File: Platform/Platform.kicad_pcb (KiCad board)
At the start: 2 copper layers, 70 x 107 mm, 0 parts

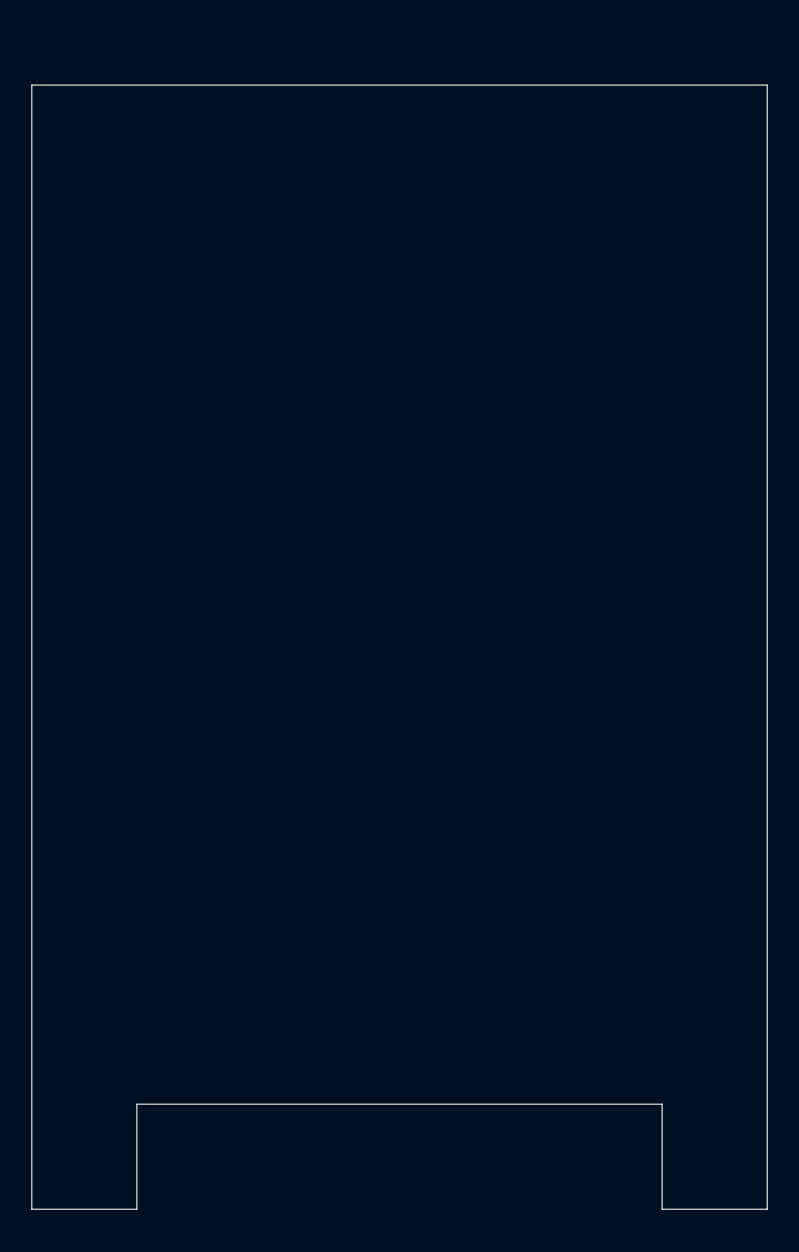
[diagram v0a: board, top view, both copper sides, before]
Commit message: Updated the PCB with component foot prints.
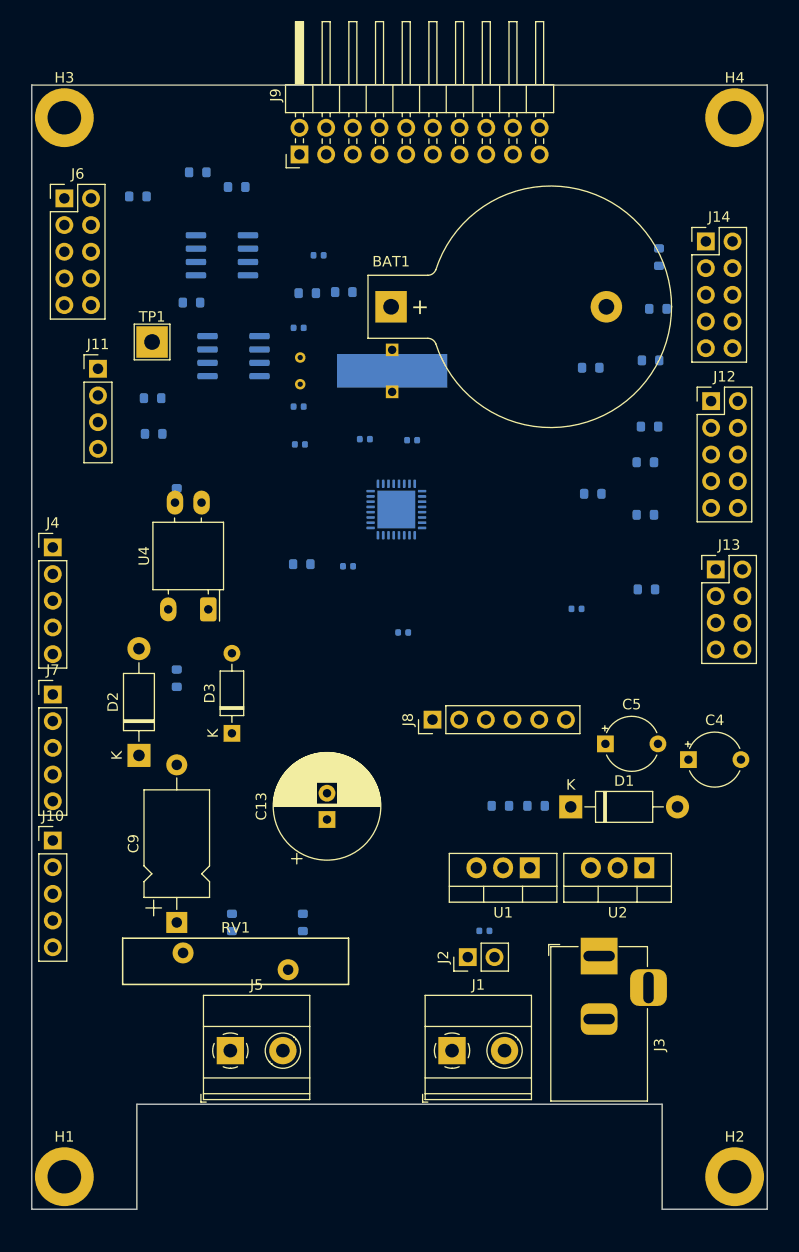
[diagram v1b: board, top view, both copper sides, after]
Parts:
- added BAT1: BS-7 3.3V, Battery:BatteryHolder_Keystone_103_1x20mm, F.Cu at (144.2, 71.2)
- added C1: 0.33uF 330NF-0402, Capacitor_SMD:C_0402_1005Metric, B.Cu at (145.3, 102.2)
- added C10: 0.1U to 1UF, Capacitor_SMD:C_0402_1005Metric, B.Cu at (137.3, 66.3)
- added C11: C_Small, Capacitor_SMD:C_0402_1005Metric, B.Cu at (135.4, 73.2)
- added C12: C_Small, Capacitor_SMD:C_0402_1005Metric, B.Cu at (135.4, 80.7)
- added C13: 2000uF, Capacitor_THT:CP_Radial_D10.0mm_P2.50mm, F.Cu at (138.1, 120.0)
- added C14: C_Small, Capacitor_SMD:C_0402_1005Metric, B.Cu at (140.1, 95.9)
- added C2: 0.1uF, Capacitor_SMD:C_0402_1005Metric, B.Cu at (161.8, 100.0)
- added C3: 0.1uF, Capacitor_SMD:C_0402_1005Metric, B.Cu at (153.1, 130.6)
- added C4: 10uF, Capacitor_THT:CP_Radial_Tantal_D5.0mm_P5.00mm, F.Cu at (172.5, 114.3)
- added C5: 1uF, Capacitor_THT:CP_Radial_Tantal_D5.0mm_P5.00mm, F.Cu at (164.6, 112.8)
- added C6: 100nF DNP, Capacitor_SMD:C_0402_1005Metric, B.Cu at (141.7, 83.8)
- added C7: 1uF, Capacitor_SMD:C_0402_1005Metric, B.Cu at (146.2, 83.9)
- added C8: 100nF DNP, Capacitor_SMD:C_0402_1005Metric, B.Cu at (135.5, 84.3)
- added C9: 0.47uF 450V AC 15mm Pitch, Capacitor_THT:CP_Axial_L10.0mm_D6.0mm_P15.00mm_Horizontal, F.Cu at (123.8, 129.8)
- added D1: 1N4001, Diode_THT:D_DO-41_SOD81_P10.16mm_Horizontal, F.Cu at (161.3, 118.8)
- added D2: DIODE IN4007, Diode_THT:D_DO-41_SOD81_P10.16mm_Horizontal, F.Cu at (120.2, 113.9)
- added D3: 5V_Zener, Diode_THT:D_DO-35_SOD27_P7.62mm_Horizontal, F.Cu at (129.1, 111.8)
- added H1: MountingHole, MountingHole:MountingHole_3.2mm_M3_DIN965_Pad, F.Cu at (113.1, 154.0)
- added H2: MountingHole, MountingHole:MountingHole_3.2mm_M3_DIN965_Pad, F.Cu at (176.9, 154.0)
- added H3: MountingHole, MountingHole:MountingHole_3.2mm_M3_DIN965_Pad, F.Cu at (113.1, 53.2)
- added H4: MountingHole, MountingHole:MountingHole_3.2mm_M3_DIN965_Pad, F.Cu at (176.9, 53.2)
- added J1: 12V INPUT, TerminalBlock_Phoenix:TerminalBlock_Phoenix_MKDS-1,5-2_1x02_P5.00mm_Horizontal, F.Cu at (150.0, 142.0)
- added J10: Conn_01x05, Connector_PinHeader_2.54mm:PinHeader_1x05_P2.54mm_Vertical, F.Cu at (112.0, 122.0)
- added J11: Relay_conn, Connector_PinHeader_2.54mm:PinHeader_1x04_P2.54mm_Vertical, F.Cu at (116.3, 77.1)
- added J12: Aardvark Header I2C, Connector_PinHeader_2.54mm:PinHeader_2x05_P2.54mm_Vertical, F.Cu at (174.7, 80.2)
- added J13: ESP8266_CONN, Connector_PinHeader_2.54mm:PinHeader_2x04_P2.54mm_Vertical, F.Cu at (175.1, 96.2)
- added J14: Aardvark Header I2C/SPI, Connector_PinHeader_2.54mm:PinHeader_2x05_P2.54mm_Vertical, F.Cu at (174.2, 65.0)
- added J2: 12V_INPUT, Connector_PinHeader_2.54mm:PinHeader_1x02_P2.54mm_Vertical, F.Cu at (151.5, 133.1)
- added J3: Barrel_Jack, Connector_BarrelJack:BarrelJack_Horizontal, F.Cu at (164.0, 133.0)
- added J4: Conn_01x05, Connector_PinHeader_2.54mm:PinHeader_1x05_P2.54mm_Vertical, F.Cu at (112.0, 94.1)
- added J5: AC INPUT, TerminalBlock_Phoenix:TerminalBlock_Phoenix_MKDS-1,5-2_1x02_P5.00mm_Horizontal, F.Cu at (128.9, 142.0)
- added J6: Debug Hdr, Connector_PinHeader_2.54mm:PinHeader_2x05_P2.54mm_Vertical, F.Cu at (113.1, 60.9)
- added J7: Conn_01x05, Connector_PinHeader_2.54mm:PinHeader_1x05_P2.54mm_Vertical, F.Cu at (112.0, 108.1)
- added J8: Conn_01x06, Connector_PinHeader_2.54mm:PinHeader_1x06_P2.54mm_Vertical, F.Cu at (148.1, 110.5)
- added J9: LED Interface, Connector_PinHeader_2.54mm:PinHeader_2x10_P2.54mm_Horizontal, F.Cu at (135.5, 56.7)
- added R1: 1K, Resistor_SMD:R_0603_1608Metric, B.Cu at (158.0, 118.7)
- added R11: 1K DNP, Resistor_SMD:R_0603_1608Metric, B.Cu at (168.4, 86.0)
- added R12: 1K DNP, Resistor_SMD:R_0603_1608Metric, B.Cu at (168.8, 82.6)
- added R13: R_Small, Resistor_SMD:R_0603_1608Metric, B.Cu at (169.7, 66.5)
- added R14: R_Small, Resistor_SMD:R_0603_1608Metric, B.Cu at (169.6, 71.4)
- added R17: 0 DNP, Resistor_SMD:R_0603_1608Metric, B.Cu at (163.4, 89.0)
- added R18: 1K, Resistor_SMD:R_0603_1608Metric, B.Cu at (168.5, 98.1)
- added R19: 0 DNP, Resistor_SMD:R_0603_1608Metric, B.Cu at (168.4, 91.0)
- added R2: 5.1K, Resistor_SMD:R_0603_1608Metric, B.Cu at (154.6, 118.7)
- added R20: 0 DNP, Resistor_SMD:R_0603_1608Metric, B.Cu at (168.9, 76.3)
- added R21: 0 DNP, Resistor_SMD:R_0603_1608Metric, B.Cu at (163.2, 77.0)
- added R25: 10K, Resistor_SMD:R_0603_1608Metric, B.Cu at (125.2, 70.8)
- added R26: 2K, Resistor_SMD:R_0603_1608Metric, B.Cu at (136.2, 69.9)
- added R27: 2K, Resistor_SMD:R_0603_1608Metric, B.Cu at (139.7, 69.8)
- added R28: 2K, Resistor_SMD:R_0603_1608Metric, B.Cu at (125.8, 58.4)
- added R29: 2K, Resistor_SMD:R_0603_1608Metric, B.Cu at (129.5, 59.8)
- added R3: 10K, Resistor_SMD:R_0603_1608Metric, B.Cu at (135.7, 95.7)
- added R30: 0E, Resistor_SMD:R_0603_1608Metric, B.Cu at (121.5, 79.9)
- added R31: 0E, Resistor_SMD:R_0603_1608Metric, B.Cu at (121.6, 83.3)
- added R4: 1K, Resistor_SMD:R_0603_1608Metric, B.Cu at (120.1, 60.7)
- added R5: R, Resistor_SMD:R_0603_1608Metric, B.Cu at (129.1, 129.8)
- added R6: R, Resistor_SMD:R_0603_1608Metric, B.Cu at (135.8, 129.8)
- added R7: R, Resistor_SMD:R_0603_1608Metric, B.Cu at (123.8, 106.5)
- added R8: 1k, Resistor_SMD:R_0603_1608Metric, B.Cu at (123.8, 89.3)
- added RV1: Varistor, Varistor:RV_Disc_D21.5mm_W4.4mm_P10mm, F.Cu at (134.4, 134.3)
- added TP1: TestPoint, TestPoint:TestPoint_THTPad_3.0x3.0mm_Drill1.5mm, F.Cu at (121.5, 74.5)
- added U1: LM7805_TO220, Package_TO_SOT_THT:TO-220-3_Vertical, F.Cu at (157.4, 124.6)
- added U2: LM317_TO-220, Package_TO_SOT_THT:TO-220-3_Vertical, F.Cu at (168.3, 124.6)
- added U3: ATSAMD21E16B-M, Package_DFN_QFN:QFN-32-1EP_5x5mm_P0.5mm_EP3.6x3.6mm, B.Cu at (144.7, 90.5)
- added U4: EL814, OptoDevice:Luna_NSL-32, F.Cu at (126.8, 100.0)
- added U5: AT24CS32-SSHM, Package_SO:SOIC-8_3.9x4.9mm_P1.27mm, B.Cu at (128.1, 66.3)
- added U6: MCP7940N-xMS, Package_SO:SOIC-8_3.9x4.9mm_P1.27mm, B.Cu at (129.2, 75.9)
- added Y1: 32KHz crystal, Crystal:Crystal_AT310_D3.0mm_L10.0mm_Horizontal_1EP_style2, B.Cu at (135.6, 76.0)

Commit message: updated the platform PCB.
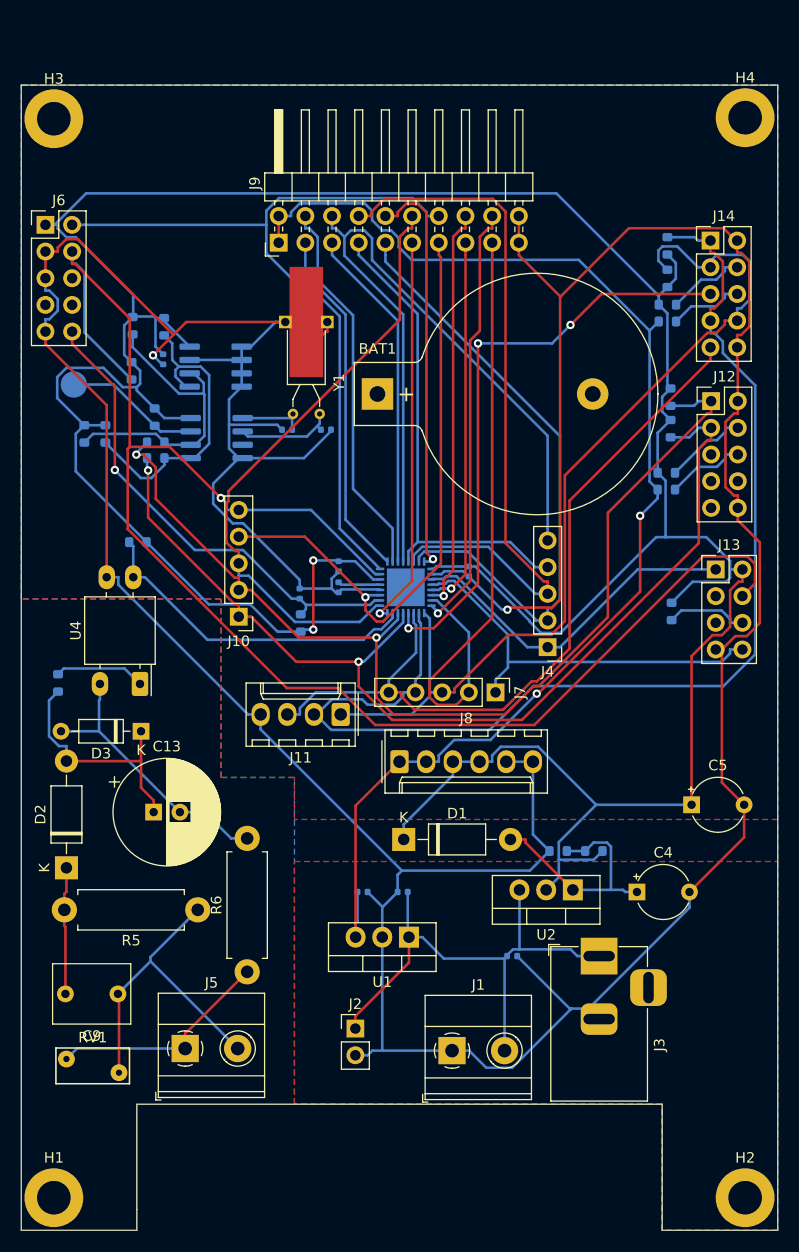
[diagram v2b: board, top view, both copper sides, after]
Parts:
- C13: value 2000uF -> 1000uF
- C9: footprint Capacitor_THT:CP_Axial_L10.0mm_D6.0mm_P15.00mm_Horizontal -> Capacitor_THT:C_Rect_L7.2mm_W5.5mm_P5.00mm_FKS2_FKP2_MKS2_MKP2
- J11: footprint Connector_PinHeader_2.54mm:PinHeader_1x04_P2.54mm_Vertical -> Connector_Molex:Molex_KK-254_AE-6410-04A_1x04_P2.54mm_Vertical
- J8: footprint Connector_PinHeader_2.54mm:PinHeader_1x06_P2.54mm_Vertical -> Connector_Molex:Molex_KK-254_AE-6410-06A_1x06_P2.54mm_Vertical
- R5: value R -> 470K 1W; footprint Resistor_SMD:R_0603_1608Metric -> Resistor_THT:R_Axial_DIN0411_L9.9mm_D3.6mm_P12.70mm_Horizontal; moved to F.Cu
- R6: value R -> 100E 1W; footprint Resistor_SMD:R_0603_1608Metric -> Resistor_THT:R_Axial_DIN0411_L9.9mm_D3.6mm_P12.70mm_Horizontal; moved to F.Cu
- R7: value R -> 220E
- RV1: footprint Varistor:RV_Disc_D21.5mm_W4.4mm_P10mm -> Varistor:RV_Disc_D7mm_W3.4mm_P5mm
- TP1: footprint TestPoint:TestPoint_THTPad_3.0x3.0mm_Drill1.5mm -> TestPoint:TestPoint_Pad_D2.5mm; moved to B.Cu
- Y1: moved to F.Cu
- moved J4 48.0 mm to (159.1, 103.6), turned to 180 degrees
- moved J7 42.1 mm to (154.1, 107.9), turned to 270 degrees
- moved J11 40.2 mm to (139.4, 110.0), turned to 180 degrees
- moved C2 33.8 mm to (141.5, 126.9)
- moved J10 27.7 mm to (129.7, 100.7), turned to 180 degrees
- moved R29 27.6 mm to (115.0, 83.3), turned to 270 degrees
- moved R28 26.4 mm to (117.0, 83.3), turned to 270 degrees
- moved C1 24.7 mm to (145.3, 126.9), turned to 180 degrees
- moved R27 20.4 mm to (119.6, 73.0), turned to 270 degrees
- moved RV1 18.8 mm to (118.3, 144.1)
- moved C10 17.8 mm to (122.5, 76.2), turned to 270 degrees
- moved R4 16.6 mm to (119.5, 77.3), turned to 270 degrees
- moved C13 16.5 mm to (121.6, 119.3), turned to 0 degrees
- moved D1 16.2 mm to (145.4, 121.9)
- moved C6 16.0 mm to (151.6, 96.4), turned to 270 degrees
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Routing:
- net GND: track 0.00 -> 421.6 mm, vias 0 -> 2
- net +3V3: track 0.00 -> 315.0 mm, vias 0 -> 2
- net PA30: track 0.00 -> 150.8 mm, vias 0 -> 1
- net +5V: track 0.00 -> 124.4 mm, vias 0 -> 2
- net PA17: track 0.00 -> 111.4 mm
- net PA23: track 0.00 -> 98.6 mm, vias 0 -> 2
- net PA22: track 0.00 -> 97.7 mm, vias 0 -> 2
- net PA16: track 0.00 -> 89.3 mm
- net PA31: track 0.00 -> 75.5 mm
- net PA03: track 0.00 -> 74.8 mm
- net PA18: track 0.00 -> 74.4 mm
- net PA05: track 0.00 -> 69.2 mm
- net PA14: track 0.00 -> 60.8 mm
- net PA06: track 0.00 -> 59.2 mm
- net PA27: track 0.00 -> 58.4 mm
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- added copper zone on F.Cu, net +12V
- added copper zone on F.Cu, net +3V3
- added copper zone on B.Cu, net GND
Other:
- board size 70 x 107 mm -> 72 x 109 mm
